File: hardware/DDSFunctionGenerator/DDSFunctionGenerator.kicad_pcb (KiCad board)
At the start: 2 copper layers, 95 x 60 mm, 130 parts, among them J1 Conn_Coaxial, J2 USB_B_Micro, J3 DG128-5.0-02P-14-00A, J4 DG128-5.0-02P-14-00A, J5 Conn_Coaxial, J6 Conn_Coaxial, J7 Conn_01x04_Male, Q1 Q_NPN_BEC, Q2 Q_NPN_BEC, Q3 Q_NPN_BEC, SW1 Rotary_Encoder_Switch, T1 Transformer_1P_1S, U1 TC1107-3.3VOA, U10 74HCT1G86, U2 L7805, U4 AD9832, U5 STM32F030K6Tx, U6 FT200XD, U7 AD8325, U8 MCP3425A0T-ECH, X1 XO91, Y1 Crystal

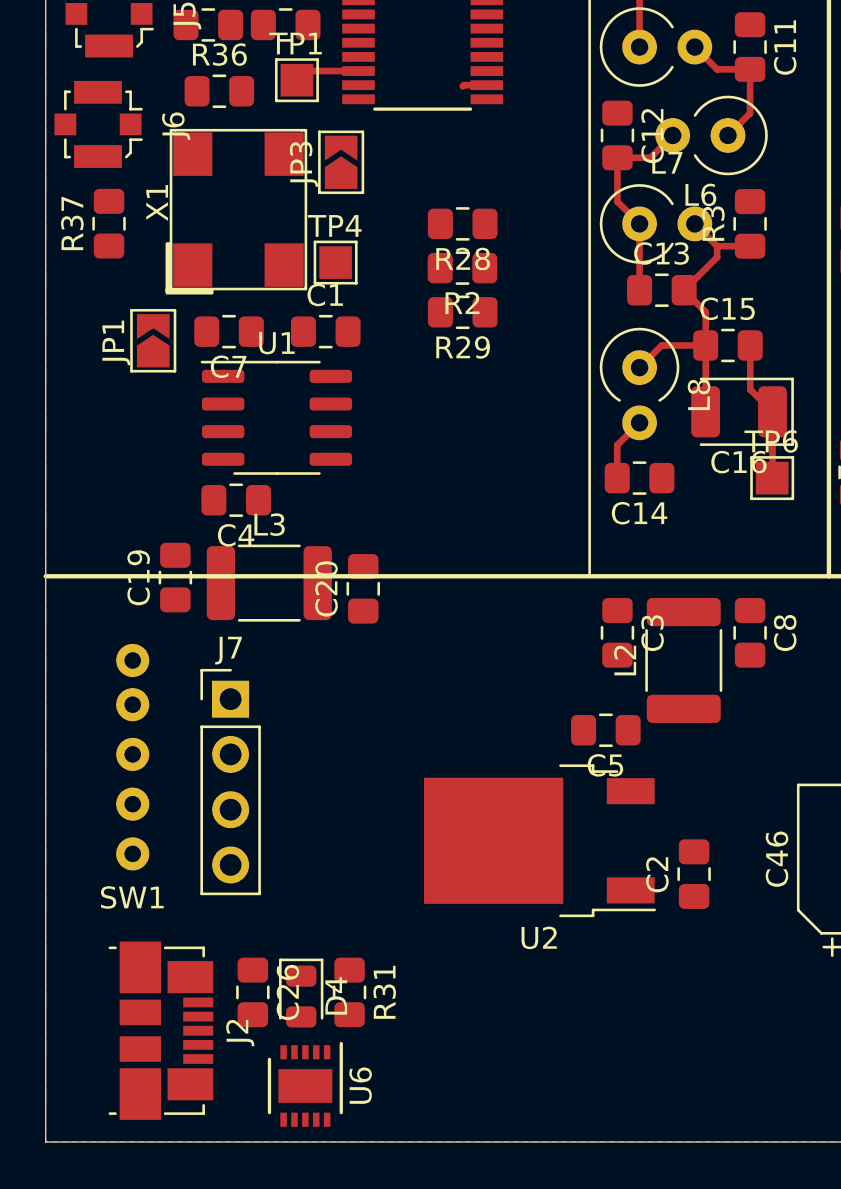
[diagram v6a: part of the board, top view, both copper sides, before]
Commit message: added missing components and connections
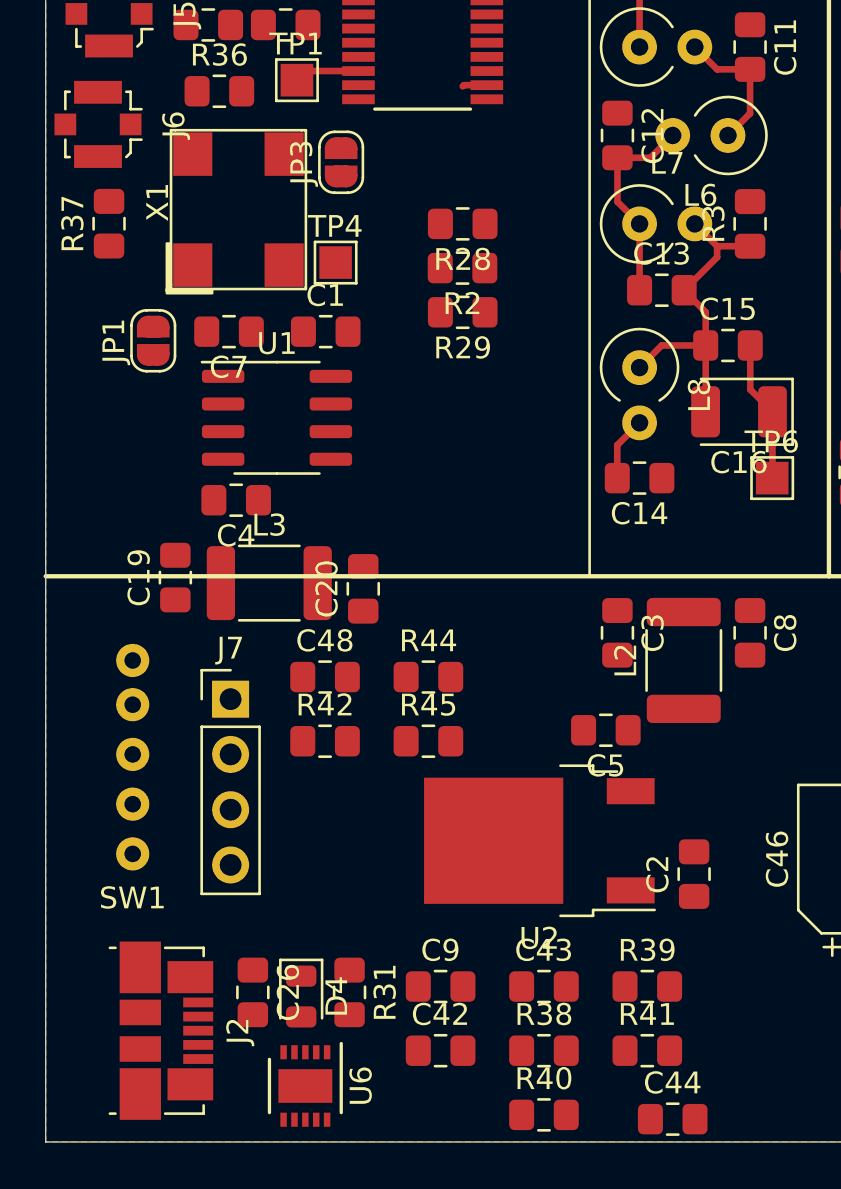
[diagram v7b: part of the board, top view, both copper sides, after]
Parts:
- added C42: 47p, Capacitor_SMD:C_0805_2012Metric_Pad1.15x1.40mm_HandSolder, F.Cu at (73.2, 120.8)
- added C43: 100n, Capacitor_SMD:C_0805_2012Metric_Pad1.15x1.40mm_HandSolder, F.Cu at (77.9, 117.9)
- added C44: 100n, Capacitor_SMD:C_0805_2012Metric_Pad1.15x1.40mm_HandSolder, F.Cu at (83.8, 124.0)
- added C48: 100n, Capacitor_SMD:C_0805_2012Metric_Pad1.15x1.40mm_HandSolder, F.Cu at (67.8, 103.6)
- added C9: 47p, Capacitor_SMD:C_0805_2012Metric_Pad1.15x1.40mm_HandSolder, F.Cu at (73.2, 117.9)
- added R38: 4k7, Resistor_SMD:R_0805_2012Metric_Pad1.15x1.40mm_HandSolder, F.Cu at (77.9, 120.8)
- added R39: 10k, Resistor_SMD:R_0805_2012Metric_Pad1.15x1.40mm_HandSolder, F.Cu at (82.7, 117.9)
- added R40: 27R, Resistor_SMD:R_0805_2012Metric_Pad1.15x1.40mm_HandSolder, F.Cu at (77.9, 123.8)
- added R41: 27R, Resistor_SMD:R_0805_2012Metric_Pad1.15x1.40mm_HandSolder, F.Cu at (82.7, 120.8)
- added R42: 10k, Resistor_SMD:R_0805_2012Metric_Pad1.15x1.40mm_HandSolder, F.Cu at (67.8, 106.6)
- added R44: 10k, Resistor_SMD:R_0805_2012Metric_Pad1.15x1.40mm_HandSolder, F.Cu at (72.6, 103.6)
- added R45: 10k, Resistor_SMD:R_0805_2012Metric_Pad1.15x1.40mm_HandSolder, F.Cu at (72.6, 106.6)
- C26: value 100n -> 10n
- JP1, JP3: footprint Jumper:SolderJumper-2_P1.3mm_Open_TrianglePad1.0x1.5mm -> Jumper:SolderJumper-2_P1.3mm_Open_RoundedPad1.0x1.5mm
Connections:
- J2 pad 2: (no net) -> Net-(C42-Pad2)
- J2 pad 3: (no net) -> Net-(C9-Pad2)
- J2 pad 4: (no net) -> GND
- J7 pad 1: (no net) -> VCC
- J7 pad 2: (no net) -> SCL
- J7 pad 3: (no net) -> SDA
- J7 pad 4: (no net) -> GND
- R32 pad 1: (no net) -> VCC
- R32 pad 2: (no net) -> SDA
- R33 pad 1: (no net) -> VCC
- R33 pad 2: (no net) -> SCL
- U5 pad 26: (no net) -> SDA
- U5 pad 27: (no net) -> SCL
- U6 pad 1: (no net) -> Net-(R40-Pad1)
- U6 pad 10: (no net) -> Net-(R41-Pad1)
- U6 pad 11: (no net) -> GND
- U6 pad 2: (no net) -> Net-(C43-Pad2)
- U6 pad 3: (no net) -> Net-(C43-Pad2)
- U6 pad 4: (no net) -> VCC
- U6 pad 5: (no net) -> Net-(R38-Pad2)
- U6 pad 6: (no net) -> SCL
- U6 pad 7: (no net) -> Net-(C43-Pad2)
- U6 pad 8: (no net) -> SDA
- U6 pad 9: (no net) -> GND
- U8 pad 3: (no net) -> SCL
- U8 pad 4: (no net) -> SDA

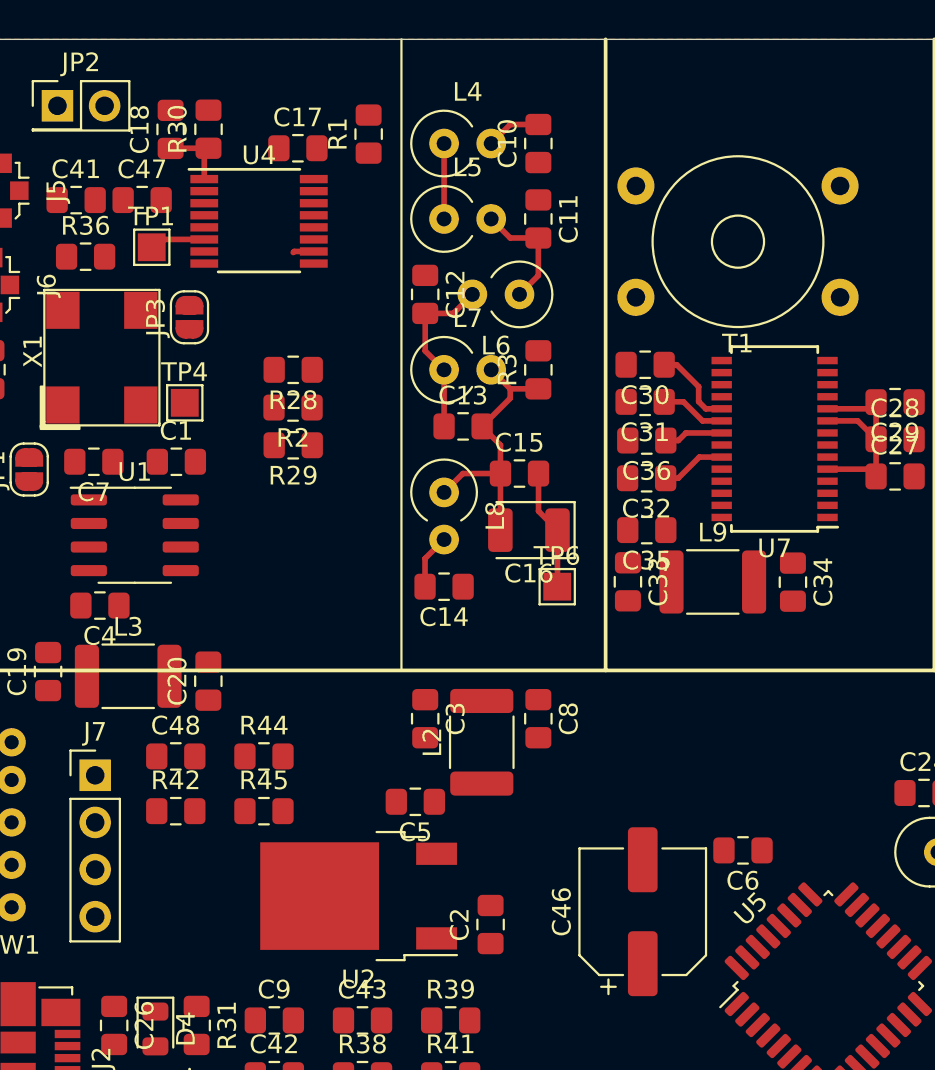
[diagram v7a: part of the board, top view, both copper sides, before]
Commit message: fix #27
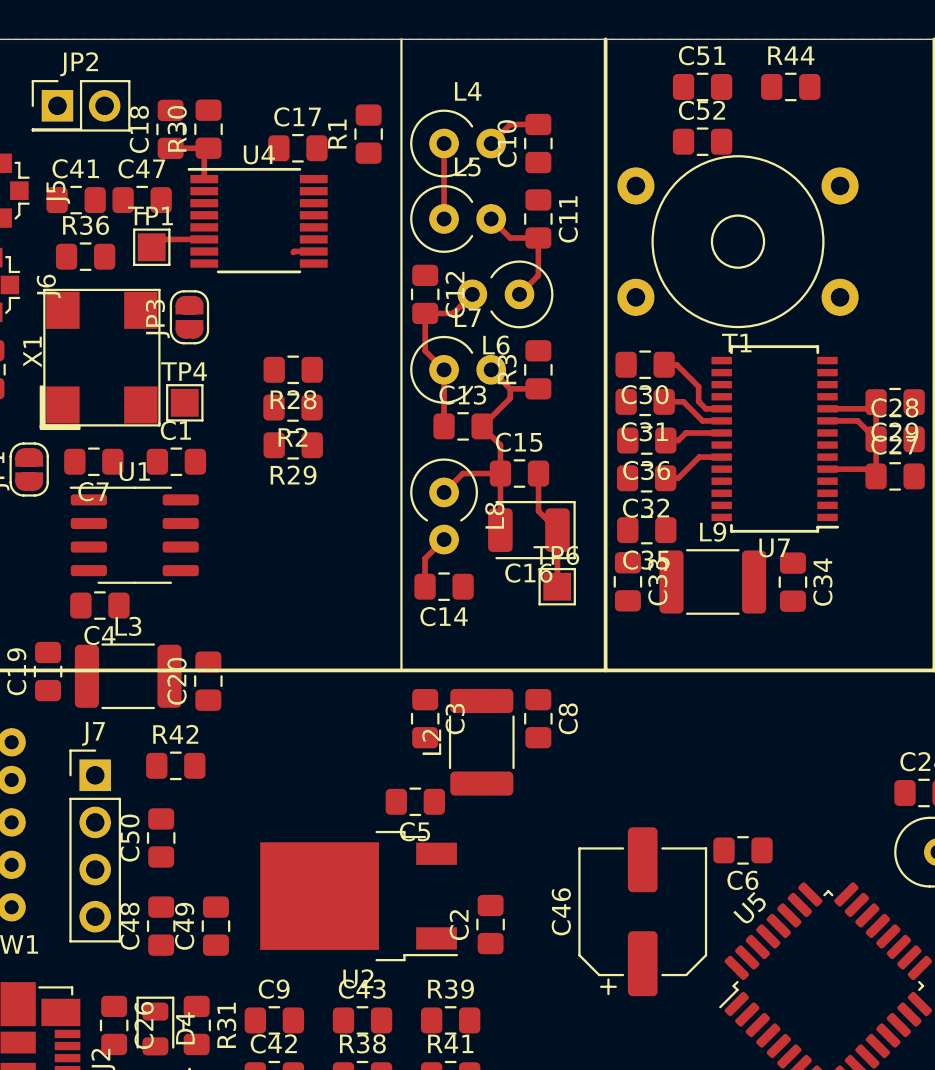
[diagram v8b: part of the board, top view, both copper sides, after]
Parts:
- removed R45: 10k, Resistor_SMD:R_0805_2012Metric_Pad1.15x1.40mm_HandSolder
- added C49: 100n, Capacitor_SMD:C_0805_2012Metric_Pad1.15x1.40mm_HandSolder, F.Cu at (70.0, 112.8)
- added C50: 100n, Capacitor_SMD:C_0805_2012Metric_Pad1.15x1.40mm_HandSolder, F.Cu at (67.1, 108.0)
- added C51: 100n, Capacitor_SMD:C_0805_2012Metric_Pad1.15x1.40mm_HandSolder, F.Cu at (96.2, 67.6)
- added C52: 100n, Capacitor_SMD:C_0805_2012Metric_Pad1.15x1.40mm_HandSolder, F.Cu at (96.2, 70.5)
- R42: value 10k -> 100R
- R44: value 10k -> 49R9
- moved R44 45.9 mm to (101.0, 67.6)
- moved C48 9.18 mm to (67.1, 112.8), turned to 90 degrees
- moved R42 2.44 mm to (67.8, 104.1)
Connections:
- C48 pad 1: (no net) -> GND
- C6 pad 1: VCC -> (no net)
- R12 pad 2: REL_2 -> (no net)
- R20 pad 2: REL_3 -> (no net)
- R4 pad 2: REL_1 -> (no net)
- R42 pad 1: (no net) -> ROT_S
- R42 pad 2: GND -> (no net)
- R44 pad 1: (no net) -> Net-(C52-Pad2)
- R44 pad 2: (no net) -> Net-(C51-Pad2)
- U4 pad 9: FSYNC -> (no net)
- U5 pad 10: CLK -> (no net)
- U5 pad 11: TXEN -> (no net)
- U5 pad 12: SLEEP -> (no net)
- U5 pad 16: (no net) -> GND
- U5 pad 2: (no net) -> Net-(C24-Pad2)
- U5 pad 20: PSEL1 -> (no net)
- U5 pad 21: PSEL0 -> (no net)
- U5 pad 22: FSELECT -> (no net)
- U5 pad 23: SDATA -> (no net)
- U5 pad 24: SCLK -> (no net)
- U5 pad 25: FSYNC -> (no net)
- U5 pad 26: SDA -> (no net)
- U5 pad 27: SCL -> (no net)
- U5 pad 28: REL_3 -> (no net)
- U5 pad 29: REL_2 -> (no net)
- U5 pad 3: (no net) -> Net-(C25-Pad2)
- U5 pad 30: REL_1 -> (no net)
- U5 pad 32: (no net) -> GND
- U5 pad 8: DATAEN -> (no net)
- U5 pad 9: SDATA -> (no net)
- U7 pad 1: DATAEN -> (no net)
- U7 pad 25: (no net) -> Net-(C52-Pad2)
- U7 pad 26: RF_DDS -> Net-(C51-Pad2)
- U7 pad 3: CLK -> SCLK
- U7 pad 6: TXEN -> (no net)
- U7 pad 7: SLEEP -> GND
